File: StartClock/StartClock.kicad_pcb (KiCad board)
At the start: 2 copper layers, 70 x 59 mm, 49 parts, among them J1 Screw_Terminal_01x05, J2 Screw_Terminal_01x02, J3 Screw_Terminal_01x02, J4 Screw_Terminal_01x02, J5 Screw_Terminal_01x04, Q1 2STR1160, Q2 2STR1160, SW1 SW_Omron_B3FS, SW2 SW_Omron_B3FS, SW3 SW_Omron_B3FS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

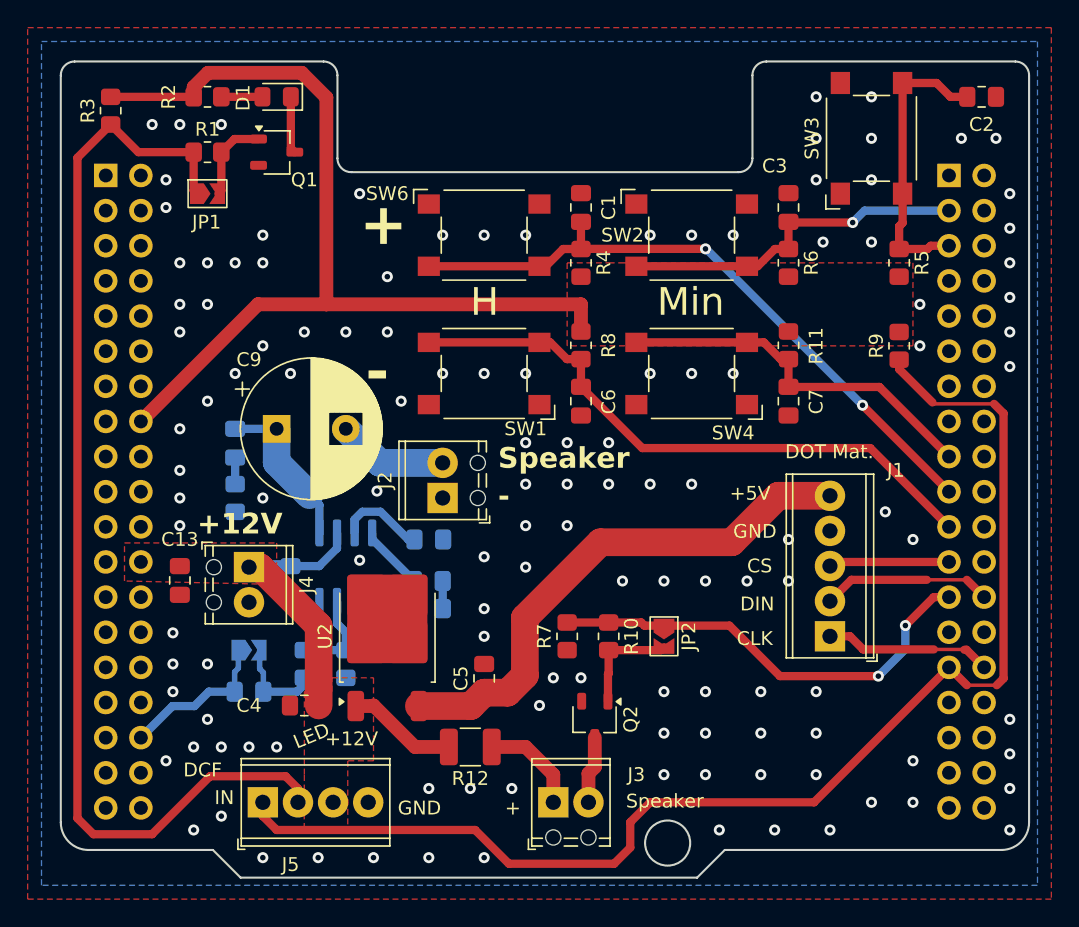
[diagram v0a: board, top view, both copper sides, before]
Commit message: Components updates after Mouser ordering few parts changed due to unavailability
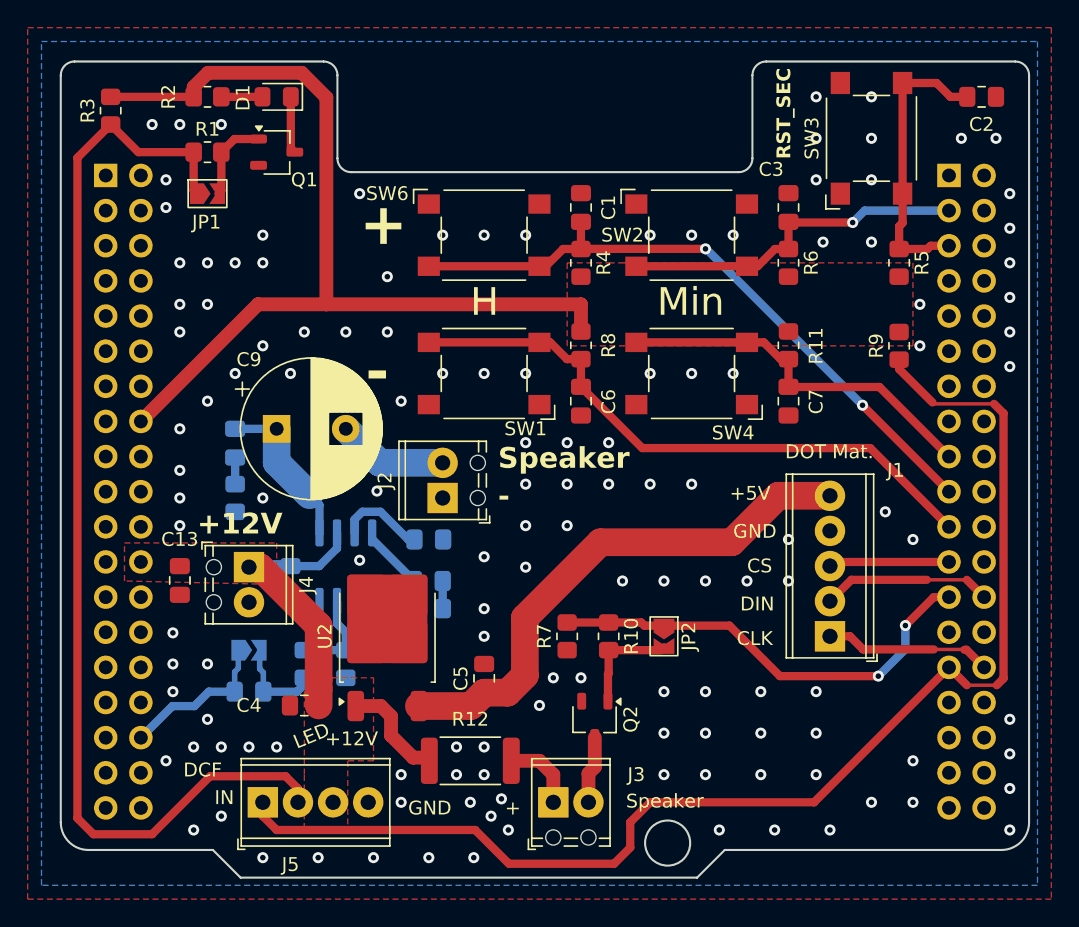
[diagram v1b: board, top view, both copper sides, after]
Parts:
- C8: value 50n -> 0.047u
- R12: footprint Resistor_SMD:R_1210_3225Metric_Pad1.30x2.65mm_HandSolder -> Resistor_SMD:R_2512_6332Metric
- moved R12 1.00 mm to (156.0, 119.0)
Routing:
- net Net-(J3-Pin_1): track 7.28 -> 5.45 mm
- net GND: vias 127 -> 134
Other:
- board text added: "RST_SEC"
